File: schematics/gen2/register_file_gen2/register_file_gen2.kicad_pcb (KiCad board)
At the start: 2 copper layers, 100 x 91.1 mm, 15 parts, among them U1 74LS02, U2 74LS02

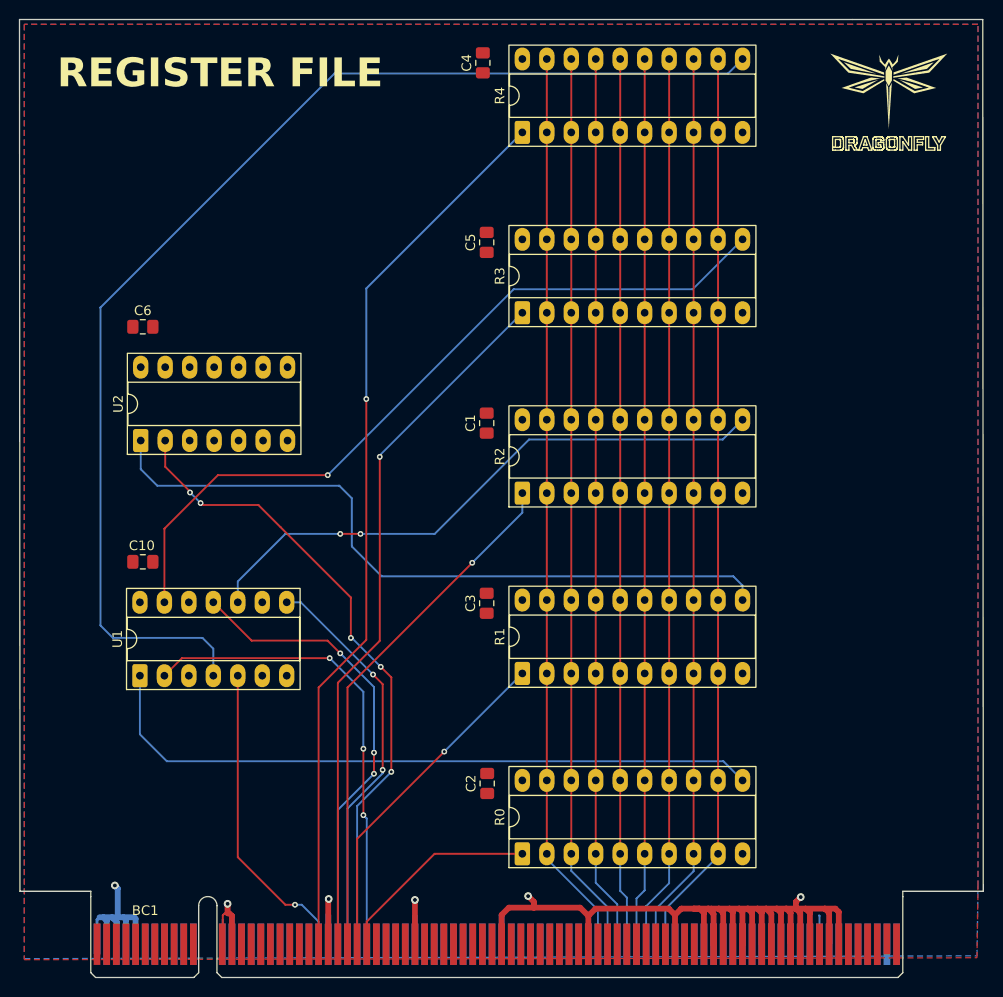
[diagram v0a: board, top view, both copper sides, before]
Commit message: fix(register file): added pull up resistor fixed schematic, changed capacitors
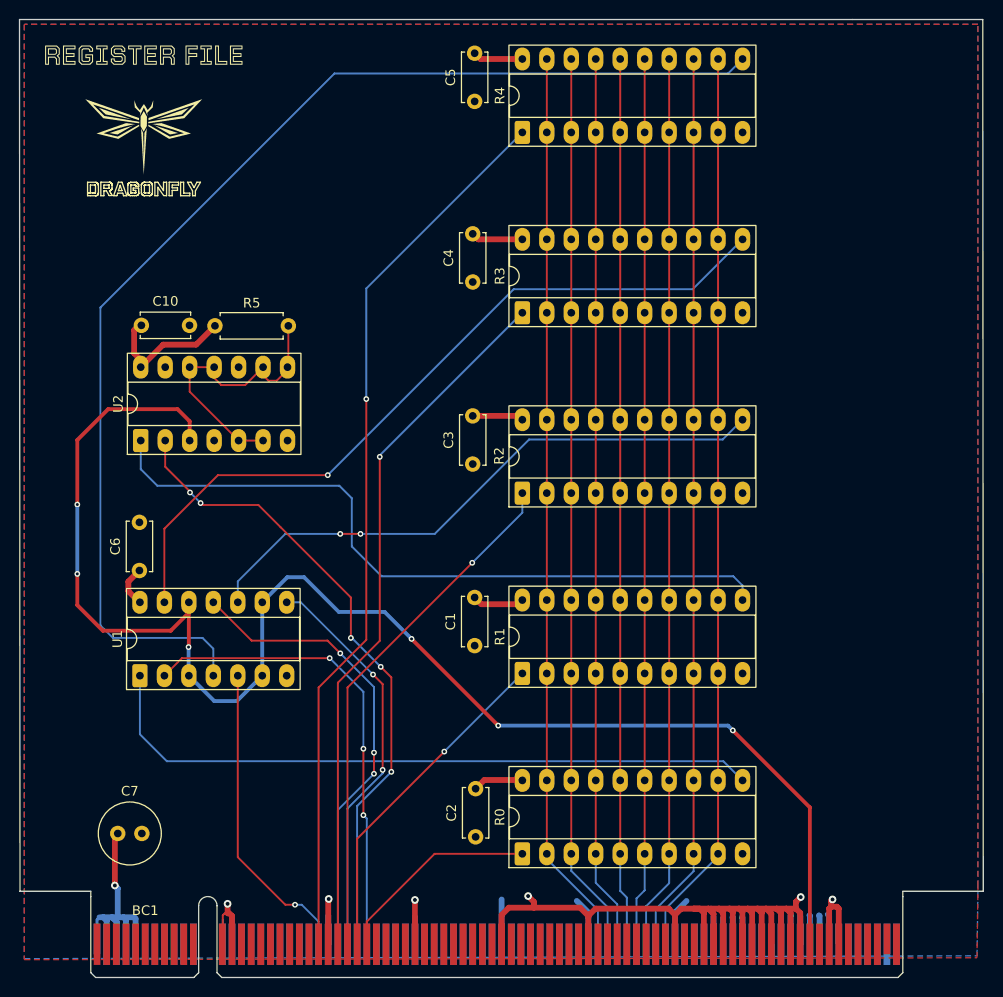
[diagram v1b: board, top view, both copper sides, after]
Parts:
- added C7: C, Capacitor_THT:C_Radial_D6.3mm_H5.0mm_P2.50mm, F.Cu at (195.1, 96.6)
- added R5: R, Resistor_THT:R_Axial_DIN0207_L6.3mm_D2.5mm_P7.62mm_Horizontal, F.Cu at (205.2, 43.9)
- added kibuzzard-6911B41A: G***, kibuzzard-6911B41A, F.Cu at (197.8, 15.8)
- C1, C10, C2, C3, C4, C5, C6: footprint Capacitor_SMD:C_0805_2012Metric_Pad1.18x1.45mm_HandSolder -> Capacitor_THT:C_Disc_D5.0mm_W2.5mm_P5.00mm
- moved C6 25.3 mm to (197.3, 69.3), turned to 90 degrees
- moved C10 24.6 mm to (197.6, 43.9)
- moved C1 23.1 mm to (232.2, 77.1)
- moved C4 22.8 mm to (231.9, 39.4)
- moved C5 14.7 mm to (232.2, 20.6)
- moved C3 14.5 mm to (231.9, 58.2)
- moved C2 5.67 mm to (232.2, 97.0)
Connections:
- BC1 pad B73: GND -> Net-(BC1-~{CLK})
- U1 pad 12: GND -> Net-(BC1-~{CLK})
- U1 pad 3: GND -> Net-(BC1-~{CLK})
- U1 pad 6: GND -> Net-(BC1-~{CLK})
- U1 pad 9: GND -> Net-(BC1-~{CLK})
- U2 pad 11: unconnected-(U2-Pad11) -> Net-(R5-Pad2)
- U2 pad 12: unconnected-(U2-Pad12) -> Net-(R5-Pad2)
- U2 pad 3: GND -> Net-(BC1-~{CLK})
- U2 pad 5: unconnected-(U2-Pad5) -> Net-(R5-Pad2)
- U2 pad 6: unconnected-(U2-Pad6) -> Net-(R5-Pad2)
- U2 pad 8: unconnected-(U2-Pad8) -> Net-(R5-Pad2)
- U2 pad 9: unconnected-(U2-Pad9) -> Net-(R5-Pad2)
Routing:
- net Net-(BC1-~{CLK}): track 0.00 -> 154.3 mm, vias 0 -> 6
- net VCC: track 21.1 -> 72.1 mm
- net Net-(R5-Pad2): track 0.00 -> 30.8 mm
- net GND: track 173.1 -> 172.7 mm, vias 5 -> 6
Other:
- board text removed: "REGISTER FILE"

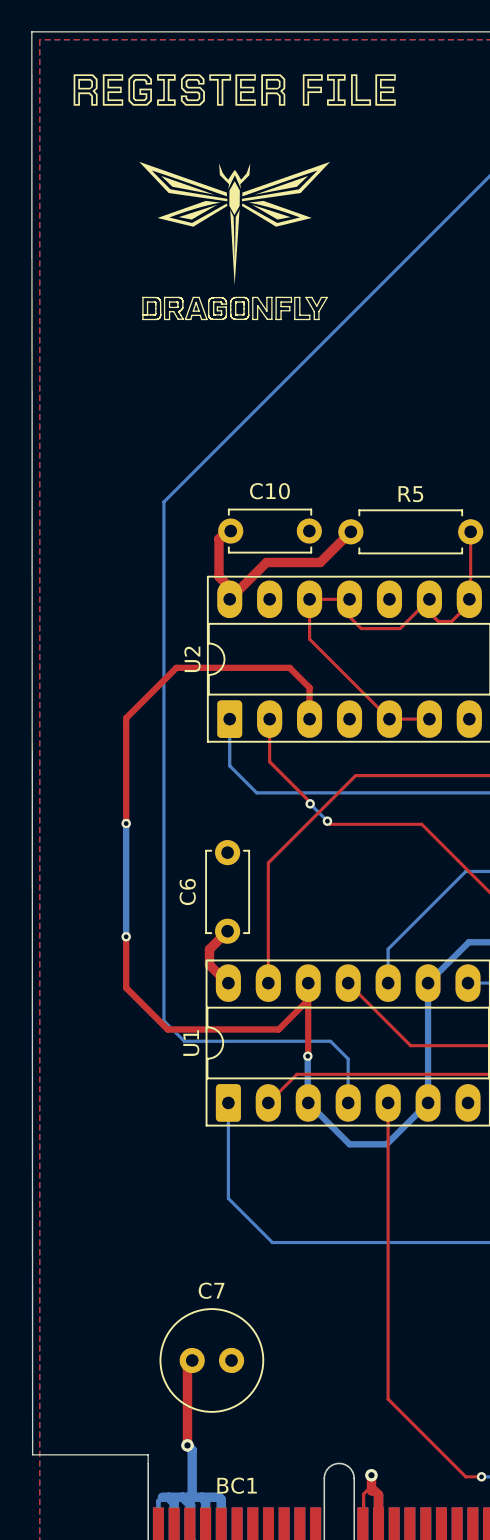
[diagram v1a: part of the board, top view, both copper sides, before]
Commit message: chore(kicad-pcb): added apps ucu logo
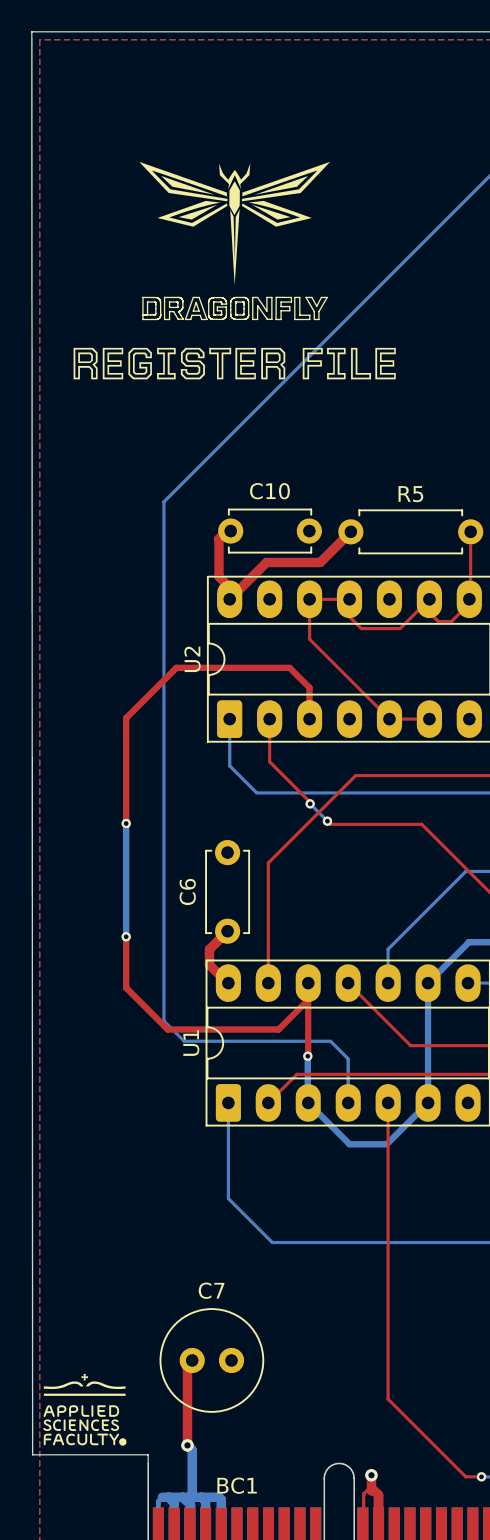
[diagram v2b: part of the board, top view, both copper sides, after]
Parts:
- moved kibuzzard-6911B41A 17.4 mm to (197.8, 33.2)

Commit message: register_file
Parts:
- moved C7 3.65 mm to (195.0, 100.2), turned to 90 degrees
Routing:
- net VCC: track 72.1 -> 68.2 mm
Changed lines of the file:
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@@
 	(footprint "Capacitor_THT:C_Radial_D6.3mm_H5.0mm_P2.50mm"
 		(layer "F.Cu")
-		(at 195.1 96.6)
+		(at 194.996016 100.246036 90)
 		(descr "C, Radial series, Radial, pin pitch=2.50mm, diameter=6.3mm, height=5mm, Non-Polar Electrolytic Capacitor")
 		(tags "C Radial series Radial pin pitch 2.50mm diameter 6.3mm height 5mm Non-Polar Electrolytic Capacitor")
 		(property "Reference" "C7"
-			(at 1.25 -4.4 0)
+			(at 5.496036 0.003984 180)
 			(layer "F.SilkS")
 			(effects
@@
 		)
 		(property "Value" "C"
-			(at 1.25 4.4 0)
+			(at 1.25 4.4 90)
 			(layer "F.Fab")
 			(effects
@@
 		)
 		(property "Datasheet" "~"
-			(at 0 0 0)
+			(at 0 0 90)
 			(layer "F.Fab")
 			(hide yes)
@@
 		)
 		(property "Description" "Unpolarized capacitor"
-			(at 0 0 0)
+			(at 0 0 90)
 			(layer "F.Fab")
 			(hide yes)
@@
 		)
 		(fp_text user "${REFERENCE}"
-			(at 1.25 0 0)
+			(at 1.25 0 90)
 			(layer "F.Fab")
 			(effects
@@
 		)
 		(pad "1" thru_hole circle
-			(at 0 0)
+			(at 0 0 90)
 			(size 1.6 1.6)
 			(drill 0.8)
@@
 		)
 		(pad "2" thru_hole circle
-			(at 2.5 0)
+			(at 2.5 0 90)
 			(size 1.6 1.6)
 			(drill 0.8)
@@
 			(pinfunction "VCC")
 			(pintype "power_in")
+			(zone_connect 0)
 		)
 		(embedded_fonts no)
@@
 			(pinfunction "VCC")
 			(pintype "power_in")
+			(zone_connect 0)
 		)
 		(embedded_fonts no)
@@
 			(pinfunction "VCC")
 			(pintype "power_in")
+			(zone_connect 0)
 		)
 		(embedded_fonts no)
@@
 			(pinfunction "VCC")
 			(pintype "power_in")
+			(zone_connect 0)
 		)
 		(embedded_fonts no)
@@
 			(pinfunction "VCC")
 			(pintype "power_in")
+			(zone_connect 0)
 		)
 		(embedded_fonts no)
@@
 			(pinfunction "VCC")
 			(pintype "power_in")
+			(zone_connect 0)
 		)
 		(embedded_fonts no)
@@
 			(pinfunction "VCC")
 			(pintype "power_in")
+			(zone_connect 0)
 		)
 		(embedded_fonts no)
@@
 	)
 	(segment
-		(start 196.2 70.45)
-		(end 196.2 71.45)
+		(start 197.485 48.19)
+		(end 197.485 47.435)
 		(width 0.6)
 		(layer "F.Cu")
@@
 	)
 	(segment
-		(start 197.485 47.435)
-		(end 196.8 46.75)
+		(start 196.2 70.45)
+		(end 196.2 71.45)
 		(width 0.6)
 		(layer "F.Cu")
@@
 	)
 	(segment
+		(start 196.8 46.75)
+		(end 196.8 44.35)
+		(width 0.6)
+		(layer "F.Cu")
+		(net 20)
+	)
+	(segment
 		(start 232.25 91.95)
 		(end 233.15 91.05)
@@
 	)
 	(segment
+		(start 199.425 46.25)
+		(end 202.84 46.25)
+		(width 0.6)
+		(layer "F.Cu")
+		(net 20)
+	)
+	(segment
 		(start 236.705 53.25)
 		(end 237.1 53.645)
@@
 	)
 	(segment
-		(start 236.6675 72.8)
-		(end 237.1 72.3675)
+		(start 197.485 48.19)
+		(end 199.425 46.25)
 		(width 0.6)
 		(layer "F.Cu")
@@
 	)
 	(segment
-		(start 233.15 91.05)
-		(end 237.06 91.05)
+		(start 236.6675 72.8)
+		(end 237.1 72.3675)
 		(width 0.6)
 		(layer "F.Cu")
@@
 	)
 	(segment
-		(start 196.8 46.75)
-		(end 196.8 44.35)
+		(start 233.15 91.05)
+		(end 237.06 91.05)
 		(width 0.6)
 		(layer "F.Cu")
@@
 	)
 	(segment
-		(start 197.485 48.19)
-		(end 199.825 45.85)
+		(start 197.485 47.435)
+		(end 196.8 46.75)
 		(width 0.6)
 		(layer "F.Cu")
@@
 	)
 	(segment
-		(start 203.24 45.85)
-		(end 205.19 43.9)
+		(start 195.1 102.3)
+		(end 195.1 100.35002)
 		(width 0.6)
 		(layer "F.Cu")
@@
 	)
 	(segment
-		(start 196.8 44.35)
-		(end 197.3 43.85)
+		(start 195.1 100.35002)
+		(end 194.996016 100.246036)
 		(width 0.6)
 		(layer "F.Cu")
@@
 	)
 	(segment
-		(start 194.8 96.9)
-		(end 195.1 96.6)
+		(start 232.75 16.2)
+		(end 232.15 15.6)
 		(width 0.6)
 		(layer "F.Cu")
@@
 	)
 	(segment
-		(start 232.75 16.2)
-		(end 232.15 15.6)
+		(start 196.8 44.35)
+		(end 197.3 43.85)
 		(width 0.6)
 		(layer "F.Cu")
@@
 	)
 	(segment
-		(start 197.485 48.19)
-		(end 197.485 47.435)
-		(width 0.2)
+		(start 202.84 46.25)
+		(end 205.19 43.9)
+		(width 0.6)
 		(layer "F.Cu")
 		(net 20)
@@
 	)
 	(segment
-		(start 194.8 102)
-		(end 194.8 96.9)
-		(width 0.6)
-		(layer "F.Cu")
-		(net 20)
-	)
-	(segment
 		(start 237.1 16.2)
 		(end 232.75 16.2)
@@
 		(net 20)
 	)
-	(segment
-		(start 199.825 45.85)
-		(end 203.24 45.85)
-		(width 0.6)
-		(layer "F.Cu")
-		(net 20)
-	)
 	(via
-		(at 194.8 102)
+		(at 195.1 102.3)
 		(size 0.8)
 		(drill 0.4)
@@
 	)
 	(segment
+		(start 195.1 102.3)
+		(end 195.1 105.3)
+		(width 0.6)
+		(layer "B.Cu")
+		(net 20)
+	)
+	(segment
 		(start 196.8 105.3)
 		(end 196.95 105.45)
@@
 	)
 	(segment
-		(start 195.1 102.3)
-		(end 194.8 102)
-		(width 0.6)
-		(layer "B.Cu")
-		(net 20)
-	)
-	(segment
 		(start 193.6 105.3)
 		(end 193.95 105.65)
 		(width 0.6)
 		(layer "B.Cu")
-		(net 20)
-	)
-	(segment
-		(start 195.1 105.3)
-		(end 195.1 102.3)
-		(width 0.6)
-		(layer "B.Cu")
